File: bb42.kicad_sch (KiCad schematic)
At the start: 90 parts, among them Q1 BSC0902NSI, Q2 BSC0902NSI, Q3 BSC0902NSI, Q4 BSC0902NSI, Q5 2N3904, U5 LM5176RHF

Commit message: format and pdf of schematic
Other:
- moved on the sheet: Q5, R27, R28, R29, TP43, TP44, TP45

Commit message: organized pdf locations
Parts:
- added D4: BAS316, Diode_SMD:D_SOD-323, symbol Diode:BAS316
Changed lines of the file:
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@@
+	)
+	(symbol
+		(lib_id "Diode:BAS316")
+		(at 100.33 24.13 0)
+		(unit 1)
+		(exclude_from_sim no)
+		(in_bom yes)
+		(on_board yes)
+		(dnp no)
+		(fields_autoplaced yes)
+		(property "Reference" "D4"
+			(at 100.33 17.78 0)
+			(effects
+				(font
+					(size 1.27 1.27)
+				)
+			)
+		)
+		(property "Value" "BAS316"
+			(at 100.33 20.32 0)
+			(effects
+				(font
+					(size 1.27 1.27)
+				)
+			)
+		)
+		(property "Footprint" "Diode_SMD:D_SOD-323"
+			(at 100.33 28.575 0)
+			(effects
+				(font
+					(size 1.27 1.27)
+				)
+				(hide yes)
+			)
+		)
+		(property "Datasheet" "https://assets.nexperia.com/documents/data-sheet/BAS16_SER.pdf"
+			(at 100.33 24.13 0)
+			(effects
+				(font
+					(size 1.27 1.27)
+				)
+				(hide yes)
+			)
+		)
+		(property "Description" "100V, 0.25A, High-speed Switching Diode, SOD-323"
+			(at 100.33 24.13 0)
+			(effects
+				(font
+					(size 1.27 1.27)
+				)
+				(hide yes)
+			)
+		)
+		(property "Sim.Device" "D"
+			(at 100.33 24.13 0)
+			(effects
+				(font
+					(size 1.27 1.27)
+				)
+				(hide yes)
+			)
+		)
+		(property "Sim.Pins" "1=K 2=A"
+			(at 100.33 24.13 0)
+			(effects
+				(font
+					(size 1.27 1.27)
+				)
+				(hide yes)
+			)
+		)
+		(pin "2"
+		)
+		(pin "1"
+		)
+		(instances
+			(project ""
+				(path "/c2919a84-19be-47b1-b680-01ad760017c4/27fcea15-03a8-4b3f-83e9-a697302f6c9b"
+					(reference "D4")
+					(unit 1)
+				)
+			)
+		)
 	)
 	(symbol

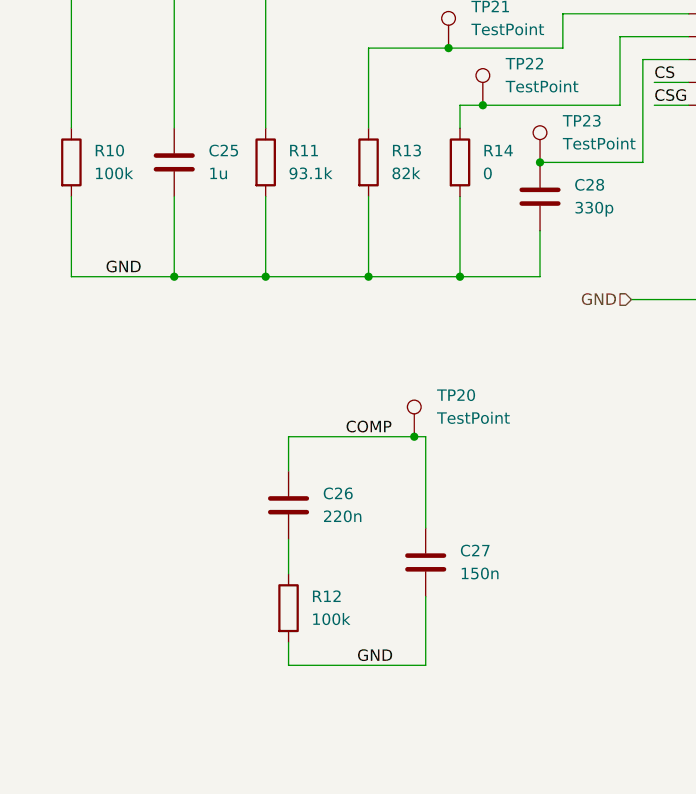
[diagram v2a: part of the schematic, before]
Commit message: rework made on v1 1st pcb for comp and ss
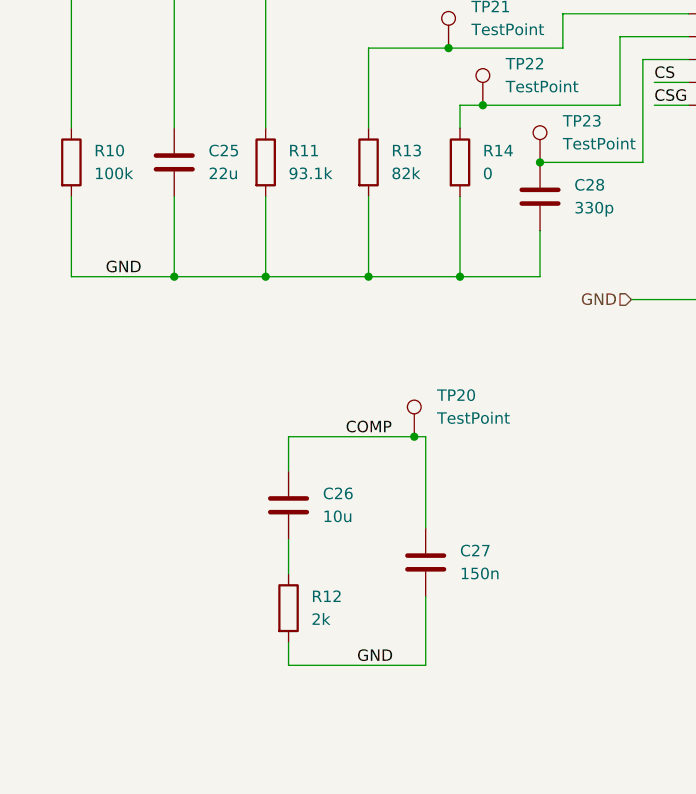
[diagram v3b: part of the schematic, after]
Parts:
- C25: value 1u -> 22u
- C26: value 220n -> 10u
- R12: value 100k -> 2k
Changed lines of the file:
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@@
 			)
 		)
-		(property "Value" "220n"
+		(property "Value" "10u"
 			(at 48.26 124.4599 0)
 			(effects
@@
 			)
 		)
-		(property "Value" "1u"
+		(property "Value" "22u"
 			(at 35.56 86.3599 0)
 			(effects
@@
 			)
 		)
-		(property "Value" "100k"
+		(property "Value" "2k"
 			(at 46.99 135.8899 0)
 			(effects

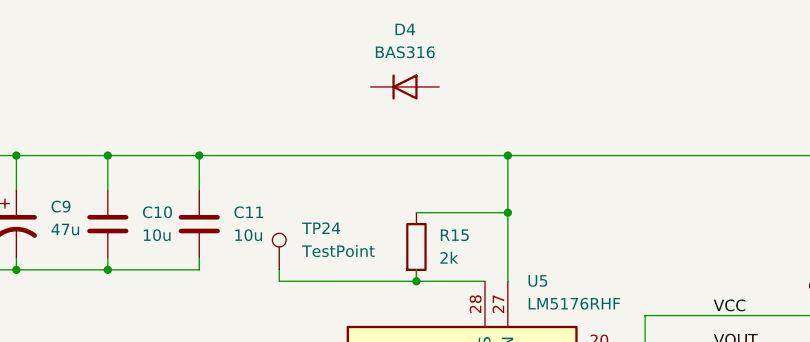
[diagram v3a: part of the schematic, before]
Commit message: removed diode net yet implemented and pdf of layout page bb
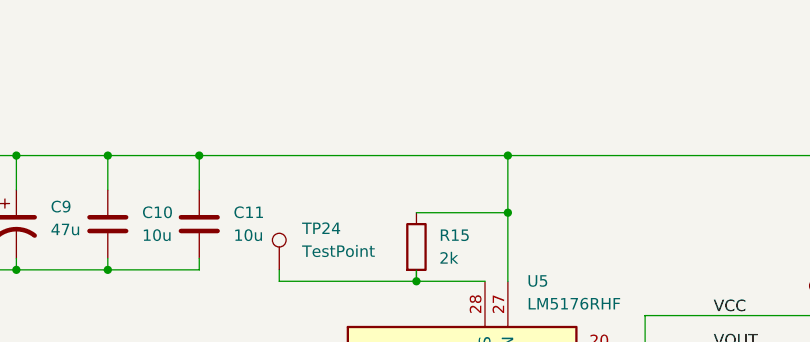
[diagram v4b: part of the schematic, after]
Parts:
- removed D4: BAS316, Diode_SMD:D_SOD-323, symbol Diode:BAS316
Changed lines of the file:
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@@
-	)
-	(symbol
-		(lib_id "Diode:BAS316")
-		(at 100.33 24.13 0)
-		(unit 1)
-		(exclude_from_sim no)
-		(in_bom yes)
-		(on_board yes)
-		(dnp no)
-		(fields_autoplaced yes)
-		(property "Reference" "D4"
-			(at 100.33 17.78 0)
-			(effects
-				(font
-					(size 1.27 1.27)
-				)
-			)
-		)
-		(property "Value" "BAS316"
-			(at 100.33 20.32 0)
-			(effects
-				(font
-					(size 1.27 1.27)
-				)
-			)
-		)
-		(property "Footprint" "Diode_SMD:D_SOD-323"
-			(at 100.33 28.575 0)
-			(effects
-				(font
-					(size 1.27 1.27)
-				)
-				(hide yes)
-			)
-		)
-		(property "Datasheet" "https://assets.nexperia.com/documents/data-sheet/BAS16_SER.pdf"
-			(at 100.33 24.13 0)
-			(effects
-				(font
-					(size 1.27 1.27)
-				)
-				(hide yes)
-			)
-		)
-		(property "Description" "100V, 0.25A, High-speed Switching Diode, SOD-323"
-			(at 100.33 24.13 0)
-			(effects
-				(font
-					(size 1.27 1.27)
-				)
-				(hide yes)
-			)
-		)
-		(property "Sim.Device" "D"
-			(at 100.33 24.13 0)
-			(effects
-				(font
-					(size 1.27 1.27)
-				)
-				(hide yes)
-			)
-		)
-		(property "Sim.Pins" "1=K 2=A"
-			(at 100.33 24.13 0)
-			(effects
-				(font
-					(size 1.27 1.27)
-				)
-				(hide yes)
-			)
-		)
-		(pin "2"
-		)
-		(pin "1"
-		)
-		(instances
-			(project ""
-				(path "/c2919a84-19be-47b1-b680-01ad760017c4/27fcea15-03a8-4b3f-83e9-a697302f6c9b"
-					(reference "D4")
-					(unit 1)
-				)
-			)
-		)
 	)
 	(symbol
